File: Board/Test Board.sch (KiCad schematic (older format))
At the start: 29 parts, among them J1 SCREW TERMINAL, J2 SCREW TERMINAL, J3 SCREW TERMINAL, K1 FINDER-32.21-x300, K2 FINDER-32.21-x300, K3 FINDER-32.21-x300, SW1 UP-MJTP1230, SW2 LT-MJTP1230, SW3 DN-MJTP1230, SW4 RT-MJTP1230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

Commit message: Begin the process of a design shrink
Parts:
- removed A1: Arduino_Nano_v3.x, Module:Arduino_Nano, symbol Test-Board-rescue:Arduino_Nano_v3.x-MCU_Module
- removed K1, K2, K3: FINDER-32.21-x300, Relay_THT:Relay_SPST_Finder_32.21-x300, symbol Relay:FINDER-32.21-x300
- added A1: Arduino_Nano_v3.x, Module:Arduino_Nano, symbol MCU_Module:Arduino_Nano_v3.x
- added U3, U4, U5: DS1E-M-DC5V, Arduino-Thermostat:DS1E-M-DC5V, symbol Arduino-Thermostat:DS1E-M-DC5V
- C1, C2: value 680uF -> 220uF; footprint Capacitor_THT:CP_Radial_D12.5mm_P5.00mm -> Capacitor_THT:CP_Radial_D10.0mm_P5.00mm
- D2: value SB5199TA -> 31DQ05TA; footprint Diode_THT:D_DO-201_P15.24mm_Horizontal -> Diode_THT:D_DO-201AD_P5.08mm_Vertical_AnodeUp
- L1: value 53uH -> 100uH
- R23: value 220R -> 600R
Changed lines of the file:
@@
 P 1450 1350
 F 0 "C1" H 1568 1396 50  0000 L CNN
-F 1 "680uF" H 1568 1305 50  0000 L CNN
-F 2 "Capacitor_THT:CP_Radial_D12.5mm_P5.00mm" H 1488 1200 50  0001 C CNN
+F 1 "220uF" H 1568 1305 50  0000 L CNN
+F 2 "Capacitor_THT:CP_Radial_D10.0mm_P5.00mm" H 1488 1200 50  0001 C CNN
 F 3 "~" H 1450 1350 50  0001 C CNN
 	1    1450 1350
@@
 P 3350 1550
 F 0 "C2" H 3468 1596 50  0000 L CNN
-F 1 "680uF" H 3468 1505 50  0000 L CNN
-F 2 "Capacitor_THT:CP_Radial_D12.5mm_P5.00mm" H 3388 1400 50  0001 C CNN
+F 1 "220uF" H 3468 1505 50  0000 L CNN
+F 2 "Capacitor_THT:CP_Radial_D10.0mm_P5.00mm" H 3388 1400 50  0001 C CNN
 F 3 "~" H 3350 1550 50  0001 C CNN
 	1    3350 1550
@@
 P 2850 1550
 F 0 "D2" V 2804 1630 50  0000 L CNN
-F 1 "SB5199TA" V 2895 1630 50  0000 L CNN
-F 2 "Diode_THT:D_DO-201_P15.24mm_Horizontal" H 2850 1550 50  0001 C CNN
+F 1 "31DQ05TA" V 2895 1630 50  0000 L CNN
+F 2 "Diode_THT:D_DO-201AD_P5.08mm_Vertical_AnodeUp" H 2850 1550 50  0001 C CNN
 F 3 "~" H 2850 1550 50  0001 C CNN
 	1    2850 1550
@@
 P 3200 1400
 F 0 "L1" V 3390 1400 50  0000 C CNN
-F 1 "53uH" V 3299 1400 50  0000 C CNN
+F 1 "100uH" V 3299 1400 50  0000 C CNN
 F 2 "Inductor_THT:L_Toroid_Vertical_L21.6mm_W11.4mm_P7.62mm_Pulse_KM-3" H 3200 1400 50  0001 C CNN
 F 3 "~" H 3200 1400 50  0001 C CNN
@@
 	1    1650 5350
 	-1   0    0    -1
-$EndComp
-$Comp
-L Test-Board-rescue:Arduino_Nano_v3.x-MCU_Module A1
-U 1 1 6118DE62
-P 10200 1800
-F 0 "A1" H 10200 711 50  0000 C CNN
-F 1 "Arduino_Nano_v3.x" H 10200 620 50  0000 C CNN
-F 2 "Module:Arduino_Nano" H 10200 1800 50  0001 C CIN
-F 3 "http://www.mouser.com/pdfdocs/Gravitech_Arduino_Nano3_0.pdf" H 10200 1800 50  0001 C CNN
-	1    10200 1800
-	1    0    0    -1
 $EndComp
 $Comp
@@
 Wire Wire Line
 	10200 4400 10350 4400
-Wire Wire Line
-	10300 2800 10200 2800
-Wire Wire Line
-	10200 2800 9800 2800
-Connection ~ 10200 2800
 $Comp
 L power:GND #PWR0120
@@
 P 5100 2300
 F 0 "R23" H 5170 2346 50  0000 L CNN
-F 1 "220R" H 5170 2255 50  0000 L CNN
+F 1 "600R" H 5170 2255 50  0000 L CNN
 F 2 "Resistor_THT:R_Axial_DIN0207_L6.3mm_D2.5mm_P7.62mm_Horizontal" V 5030 2300 50  0001 C CNN
 F 3 "~" H 5100 2300 50  0001 C CNN
@@
 	0    -1   -1   0
 $EndComp
-$Comp
-L Relay:FINDER-32.21-x300 K1
-U 1 1 612C8E7E
-P 3800 4300
-F 0 "K1" H 4230 4346 50  0000 L CNN
-F 1 "FINDER-32.21-x300" H 4230 4255 50  0000 L CNN
-F 2 "Relay_THT:Relay_SPST_Finder_32.21-x300" H 5070 4270 50  0001 C CNN
-F 3 "http://gfinder.findernet.com/assets/Series/355/S32EN.pdf" H 3800 4300 50  0001 C CNN
-	1    3800 4300
-	1    0    0    -1
-$EndComp
-$Comp
-L Relay:FINDER-32.21-x300 K3
-U 1 1 612D0CAA
-P 3800 6300
-F 0 "K3" H 4230 6346 50  0000 L CNN
-F 1 "FINDER-32.21-x300" H 4230 6255 50  0000 L CNN
-F 2 "Relay_THT:Relay_SPST_Finder_32.21-x300" H 5070 6270 50  0001 C CNN
-F 3 "http://gfinder.findernet.com/assets/Series/355/S32EN.pdf" H 3800 6300 50  0001 C CNN
-	1    3800 6300
-	1    0    0    -1
-$EndComp
-$Comp
-L Relay:FINDER-32.21-x300 K2
-U 1 1 612D5FFC
-P 3800 5300
-F 0 "K2" H 4230 5346 50  0000 L CNN
-F 1 "FINDER-32.21-x300" H 4230 5255 50  0000 L CNN
-F 2 "Relay_THT:Relay_SPST_Finder_32.21-x300" H 5070 5270 50  0001 C CNN
-F 3 "http://gfinder.findernet.com/assets/Series/355/S32EN.pdf" H 3800 5300 50  0001 C CNN
-	1    3800 5300
-	1    0    0    -1
-$EndComp
-Text Label 4250 4000 0    50   ~ 0
+Text Label 4300 4750 0    50   ~ 0
 R
-Text Label 4250 5000 0    50   ~ 0
+Text Label 4300 6100 0    50   ~ 0
 R
-Text Label 4250 6000 0    50   ~ 0
-R
-Wire Wire Line
-	4100 6000 4250 6000
-Wire Wire Line
-	4100 5000 4250 5000
-Wire Wire Line
-	4100 4000 4250 4000
+Wire Wire Line
+	4150 6100 4300 6100
+Wire Wire Line
+	4150 4750 4300 4750
 $Comp
 L power:GND #PWR03
 U 1 1 6132FB03
-P 3600 6600
-F 0 "#PWR03" H 3600 6350 50  0001 C CNN
-F 1 "GND" H 3605 6427 50  0000 C CNN
-F 2 "" H 3600 6600 50  0001 C CNN
-F 3 "" H 3600 6600 50  0001 C CNN
-	1    3600 6600
-	1    0    0    -1
-$EndComp
-$Comp
-L power:GND #PWR02
-U 1 1 613309E2
-P 3600 5600
-F 0 "#PWR02" H 3600 5350 50  0001 C CNN
-F 1 "GND" H 3605 5427 50  0000 C CNN
-F 2 "" H 3600 5600 50  0001 C CNN
-F 3 "" H 3600 5600 50  0001 C CNN
-	1    3600 5600
+P 3800 7100
+F 0 "#PWR03" H 3800 6850 50  0001 C CNN
+F 1 "GND" H 3805 6927 50  0000 C CNN
+F 2 "" H 3800 7100 50  0001 C CNN
+F 3 "" H 3800 7100 50  0001 C CNN
+	1    3800 7100
 	1    0    0    -1
 $EndComp
@@
 L power:GND #PWR01
 U 1 1 61331D39
-P 3600 4600
-F 0 "#PWR01" H 3600 4350 50  0001 C CNN
-F 1 "GND" H 3605 4427 50  0000 C CNN
-F 2 "" H 3600 4600 50  0001 C CNN
-F 3 "" H 3600 4600 50  0001 C CNN
-	1    3600 4600
-	1    0    0    -1
-$EndComp
-Text Label 3900 4000 2    50   ~ 0
+P 3800 4400
+F 0 "#PWR01" H 3800 4150 50  0001 C CNN
+F 1 "GND" H 3805 4227 50  0000 C CNN
+F 2 "" H 3800 4400 50  0001 C CNN
+F 3 "" H 3800 4400 50  0001 C CNN
+	1    3800 4400
+	1    0    0    -1
+$EndComp
+Text Label 3500 3400 0    50   ~ 0
 FANRLY
-Text Label 3900 5000 2    50   ~ 0
+Text Label 3500 4750 0    50   ~ 0
 HEATRLY
-Text Label 3900 6000 2    50   ~ 0
+Text Label 3500 6100 0    50   ~ 0
 COOLRLY
 Text Label 7450 5000 2    50   ~ 0
@@
 	7050 4400 7450 4400
 Wire Wire Line
-	3600 4000 3900 4000
-Wire Wire Line
-	3600 5000 3900 5000
-Wire Wire Line
-	3600 6000 3900 6000
-Text Label 4000 6700 0    50   ~ 0
+	3800 3400 3500 3400
+Wire Wire Line
+	3800 4750 3500 4750
+Wire Wire Line
+	3800 6100 3500 6100
+Text Label 4050 7200 0    50   ~ 0
 Y
 Wire Wire Line
-	4000 6600 4000 6700
-Wire Wire Line
-	4000 5700 4000 5600
-Text Label 4000 5700 0    50   ~ 0
-W
-Text Label 4000 4700 0    50   ~ 0
+	4050 7100 4050 7200
+Text Label 4050 4500 0    50   ~ 0
 G
-Wire Wire Line
-	4000 4600 4000 4700
 $Comp
 L Connector:Screw_Terminal_01x02 J2
@@
 	0    -1   -1   0
 $EndComp
+$Comp
+L Arduino-Thermostat:DS1E-M-DC5V U3
+U 1 1 61909F87
+P 3500 5600
+F 0 "U3" V 5253 4852 60  0000 R CNN
+F 1 "DS1E-M-DC5V" V 5147 4852 60  0000 R CNN
+F 2 "Arduino-Thermostat:DS1E-M-DC5V" H 5200 5640 60  0001 C CNN
+F 3 "" H 4700 5300 60  0000 C CNN
+	1    3500 5600
+	0    -1   -1   0
+$EndComp
+Wire Wire Line
+	4050 4400 4050 4500
+Wire Wire Line
+	4150 3400 4300 3400
+Text Label 4300 3400 0    50   ~ 0
+R
+$Comp
+L Arduino-Thermostat:DS1E-M-DC5V U5
+U 1 1 619468A4
+P 3500 8300
+F 0 "U5" V 5253 7552 60  0000 R CNN
+F 1 "DS1E-M-DC5V" V 5147 7552 60  0000 R CNN
+F 2 "Arduino-Thermostat:DS1E-M-DC5V" H 5200 8340 60  0001 C CNN
+F 3 "" H 4700 8000 60  0000 C CNN
+	1    3500 8300
+	0    -1   -1   0
+$EndComp
+$Comp
+L Arduino-Thermostat:DS1E-M-DC5V U4
+U 1 1 6192B6E5
+P 3500 6950
+F 0 "U4" V 5253 6202 60  0000 R CNN
+F 1 "DS1E-M-DC5V" V 5147 6202 60  0000 R CNN
+F 2 "Arduino-Thermostat:DS1E-M-DC5V" H 5200 6990 60  0001 C CNN
+F 3 "" H 4700 6650 60  0000 C CNN
+	1    3500 6950
+	0    -1   -1   0
+$EndComp
+Text Label 4050 5850 0    50   ~ 0
+W
+Wire Wire Line
+	4050 5850 4050 5750
+$Comp
+L power:GND #PWR02
+U 1 1 613309E2
+P 3800 5750
+F 0 "#PWR02" H 3800 5500 50  0001 C CNN
+F 1 "GND" H 3805 5577 50  0000 C CNN
+F 2 "" H 3800 5750 50  0001 C CNN
+F 3 "" H 3800 5750 50  0001 C CNN
+	1    3800 5750
+	1    0    0    -1
+$EndComp
+Wire Wire Line
+	9800 2800 10200 2800
+$Comp
+L MCU_Module:Arduino_Nano_v3.x A1
+U 1 1 61970FE6
+P 10200 1800
+F 0 "A1" H 10200 711 50  0000 C CNN
+F 1 "Arduino_Nano_v3.x" H 10200 620 50  0000 C CNN
+F 2 "Module:Arduino_Nano" H 10200 1800 50  0001 C CIN
+F 3 "http://www.mouser.com/pdfdocs/Gravitech_Arduino_Nano3_0.pdf" H 10200 1800 50  0001 C CNN
+	1    10200 1800
+	1    0    0    -1
+$EndComp
+Wire Wire Line
+	10200 2800 10300 2800
+Connection ~ 10200 2800
 $EndSCHEMATC

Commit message: Started re-engineering board
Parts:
- L1: value 100uH -> 53uH; footprint Inductor_THT:L_Toroid_Vertical_L21.6mm_W11.4mm_P7.62mm_Pulse_KM-3 -> Inductor_THT:L_Radial_D12.0mm_P5.00mm_Fastron_11P
- R1: value 220R -> XXR; footprint Resistor_THT:R_Axial_DIN0207_L6.3mm_D2.5mm_P7.62mm_Horizontal -> Resistor_SMD:R_1206_3216Metric
- R18, R19, R20, R21, R22, R23: footprint Resistor_THT:R_Axial_DIN0207_L6.3mm_D2.5mm_P7.62mm_Horizontal -> Resistor_SMD:R_1206_3216Metric
- U6: footprint Sensor:Aosong_DHT11_5.5x12.0_P2.54mm -> Arduino-Thermostat:DHT22-Horizontal
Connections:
- no-connect marks 17 -> 20
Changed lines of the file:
@@
 P 3200 1400
 F 0 "L1" V 3390 1400 50  0000 C CNN
-F 1 "100uH" V 3299 1400 50  0000 C CNN
-F 2 "Inductor_THT:L_Toroid_Vertical_L21.6mm_W11.4mm_P7.62mm_Pulse_KM-3" H 3200 1400 50  0001 C CNN
+F 1 "53uH" V 3299 1400 50  0000 C CNN
+F 2 "Inductor_THT:L_Radial_D12.0mm_P5.00mm_Fastron_11P" H 3200 1400 50  0001 C CNN
 F 3 "~" H 3200 1400 50  0001 C CNN
 	1    3200 1400
@@
 F 0 "U6" V 9819 3750 50  0000 C CNN
 F 1 "DHT11" V 9910 3750 50  0000 C CNN
-F 2 "Sensor:Aosong_DHT11_5.5x12.0_P2.54mm" H 10200 3350 50  0001 C CNN
+F 2 "Arduino-Thermostat:DHT22-Horizontal" H 10200 3350 50  0001 C CNN
 F 3 "http://akizukidenshi.com/download/ds/aosong/DHT11.pdf" H 10350 4000 50  0001 C CNN
 	1    10200 3750
@@
 F 0 "R22" V 9843 4250 50  0000 C CNN
 F 1 "10k" V 9934 4250 50  0000 C CNN
-F 2 "Resistor_THT:R_Axial_DIN0207_L6.3mm_D2.5mm_P7.62mm_Horizontal" V 9980 4250 50  0001 C CNN
+F 2 "Resistor_SMD:R_1206_3216Metric" V 9980 4250 50  0001 C CNN
 F 3 "~" H 10050 4250 50  0001 C CNN
 	1    10050 4250
@@
 F 0 "R20" H 10020 5096 50  0000 L CNN
 F 1 "47k" H 10020 5005 50  0000 L CNN
-F 2 "Resistor_THT:R_Axial_DIN0207_L6.3mm_D2.5mm_P7.62mm_Horizontal" V 9880 5050 50  0001 C CNN
+F 2 "Resistor_SMD:R_1206_3216Metric" V 9880 5050 50  0001 C CNN
 F 3 "~" H 9950 5050 50  0001 C CNN
 	1    9950 5050
@@
 F 0 "R18" H 8870 5096 50  0000 L CNN
 F 1 "47k" H 8870 5005 50  0000 L CNN
-F 2 "Resistor_THT:R_Axial_DIN0207_L6.3mm_D2.5mm_P7.62mm_Horizontal" V 8730 5050 50  0001 C CNN
+F 2 "Resistor_SMD:R_1206_3216Metric" V 8730 5050 50  0001 C CNN
 F 3 "~" H 8800 5050 50  0001 C CNN
 	1    8800 5050
@@
 F 0 "R19" H 8870 5796 50  0000 L CNN
 F 1 "47k" H 8870 5705 50  0000 L CNN
-F 2 "Resistor_THT:R_Axial_DIN0207_L6.3mm_D2.5mm_P7.62mm_Horizontal" V 8730 5750 50  0001 C CNN
+F 2 "Resistor_SMD:R_1206_3216Metric" V 8730 5750 50  0001 C CNN
 F 3 "~" H 8800 5750 50  0001 C CNN
 	1    8800 5750
@@
 F 0 "R21" H 10020 5796 50  0000 L CNN
 F 1 "47k" H 10020 5705 50  0000 L CNN
-F 2 "Resistor_THT:R_Axial_DIN0207_L6.3mm_D2.5mm_P7.62mm_Horizontal" V 9880 5750 50  0001 C CNN
+F 2 "Resistor_SMD:R_1206_3216Metric" V 9880 5750 50  0001 C CNN
 F 3 "~" H 9950 5750 50  0001 C CNN
 	1    9950 5750
@@
 F 0 "R23" H 5170 2346 50  0000 L CNN
 F 1 "600R" H 5170 2255 50  0000 L CNN
-F 2 "Resistor_THT:R_Axial_DIN0207_L6.3mm_D2.5mm_P7.62mm_Horizontal" V 5030 2300 50  0001 C CNN
+F 2 "Resistor_SMD:R_1206_3216Metric" V 5030 2300 50  0001 C CNN
 F 3 "~" H 5100 2300 50  0001 C CNN
 	1    5100 2300
@@
 P 7700 1900
 F 0 "R1" V 7907 1900 50  0000 C CNN
-F 1 "220R" V 7816 1900 50  0000 C CNN
-F 2 "Resistor_THT:R_Axial_DIN0207_L6.3mm_D2.5mm_P7.62mm_Horizontal" V 7630 1900 50  0001 C CNN
+F 1 "XXR" V 7816 1900 50  0000 C CNN
+F 2 "Resistor_SMD:R_1206_3216Metric" V 7630 1900 50  0001 C CNN
 F 3 "~" H 7700 1900 50  0001 C CNN
 	1    7700 1900
@@
 	10200 2800 10300 2800
 Connection ~ 10200 2800
+NoConn ~ 3900 3400
+NoConn ~ 3900 4750
+NoConn ~ 3900 6100
 $EndSCHEMATC

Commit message: Added E-Ink Display files
Started making E-Ink Display footprints
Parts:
- removed DS1: WC1602A, Display:WC1602A, symbol Display_Character:WC1602A
- removed R1: XXR, Resistor_SMD:R_1206_3216Metric, symbol Device:R
- removed R18, R19, R20, R21: 47k, Resistor_SMD:R_1206_3216Metric, symbol Device:R
- removed RV1: 10k, Potentiometer_THT:Potentiometer_Bourns_3266Y_Vertical, symbol Device:R_POT
- removed SW1: UP-MJTP1230, Button_Switch_THT:SW_PUSH_6mm, symbol Switch:SW_Push
- removed SW2: LT-MJTP1230, Button_Switch_THT:SW_PUSH_6mm, symbol Switch:SW_Push
- removed SW3: DN-MJTP1230, Button_Switch_THT:SW_PUSH_6mm, symbol Switch:SW_Push
- removed SW4: RT-MJTP1230, Button_Switch_THT:SW_PUSH_6mm, symbol Switch:SW_Push
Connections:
- wire segments 87 -> 65
- no-connect marks 20 -> 16
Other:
- moved on the sheet: D3, R23, U2

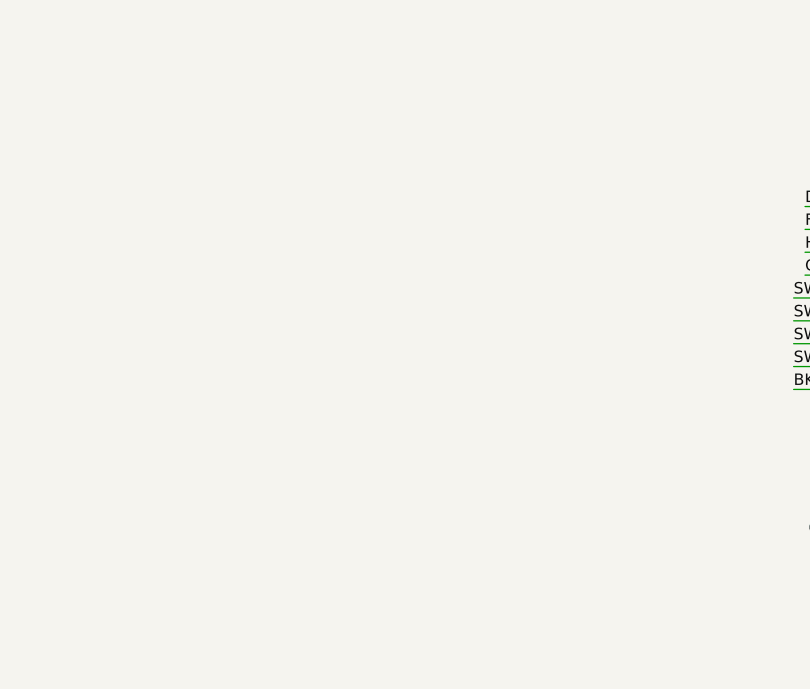
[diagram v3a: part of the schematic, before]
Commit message: Finished E-Ink Footprint
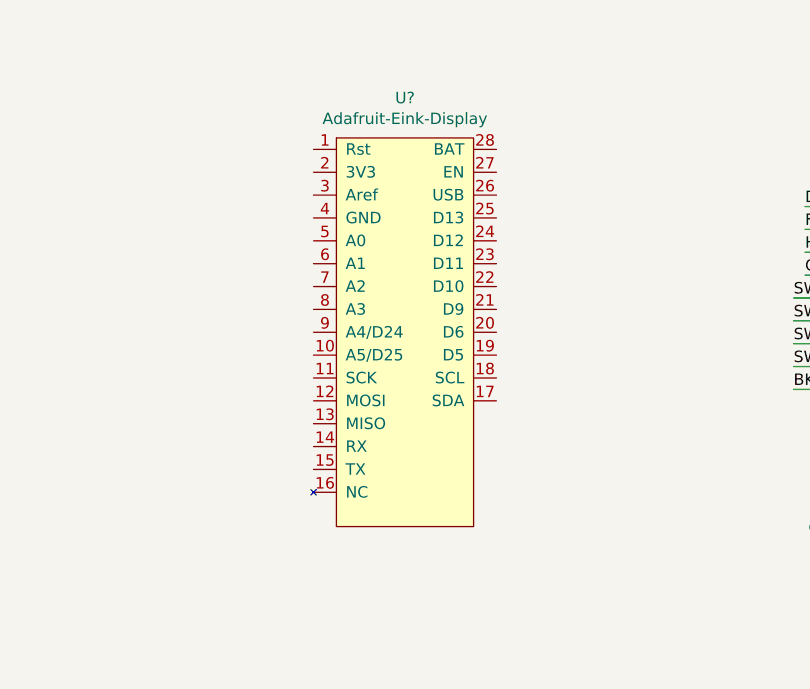
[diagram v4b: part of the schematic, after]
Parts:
- added U?: Adafruit-Eink-Display, symbol Arduino-Thermostat:Adafruit-Eink-Display
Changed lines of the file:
@@
 NoConn ~ 3900 4750
 NoConn ~ 3900 6100
+$Comp
+L Arduino-Thermostat:Adafruit-Eink-Display U?
+U 1 1 61ED981D
+P 7750 1050
+F 0 "U?" H 7750 1175 50  0000 C CNN
+F 1 "Adafruit-Eink-Display" H 7750 1084 50  0000 C CNN
+F 2 "" H 7750 1050 50  0001 C CNN
+F 3 "" H 7750 1050 50  0001 C CNN
+	1    7750 1050
+	1    0    0    -1
+$EndComp
 $EndSCHEMATC

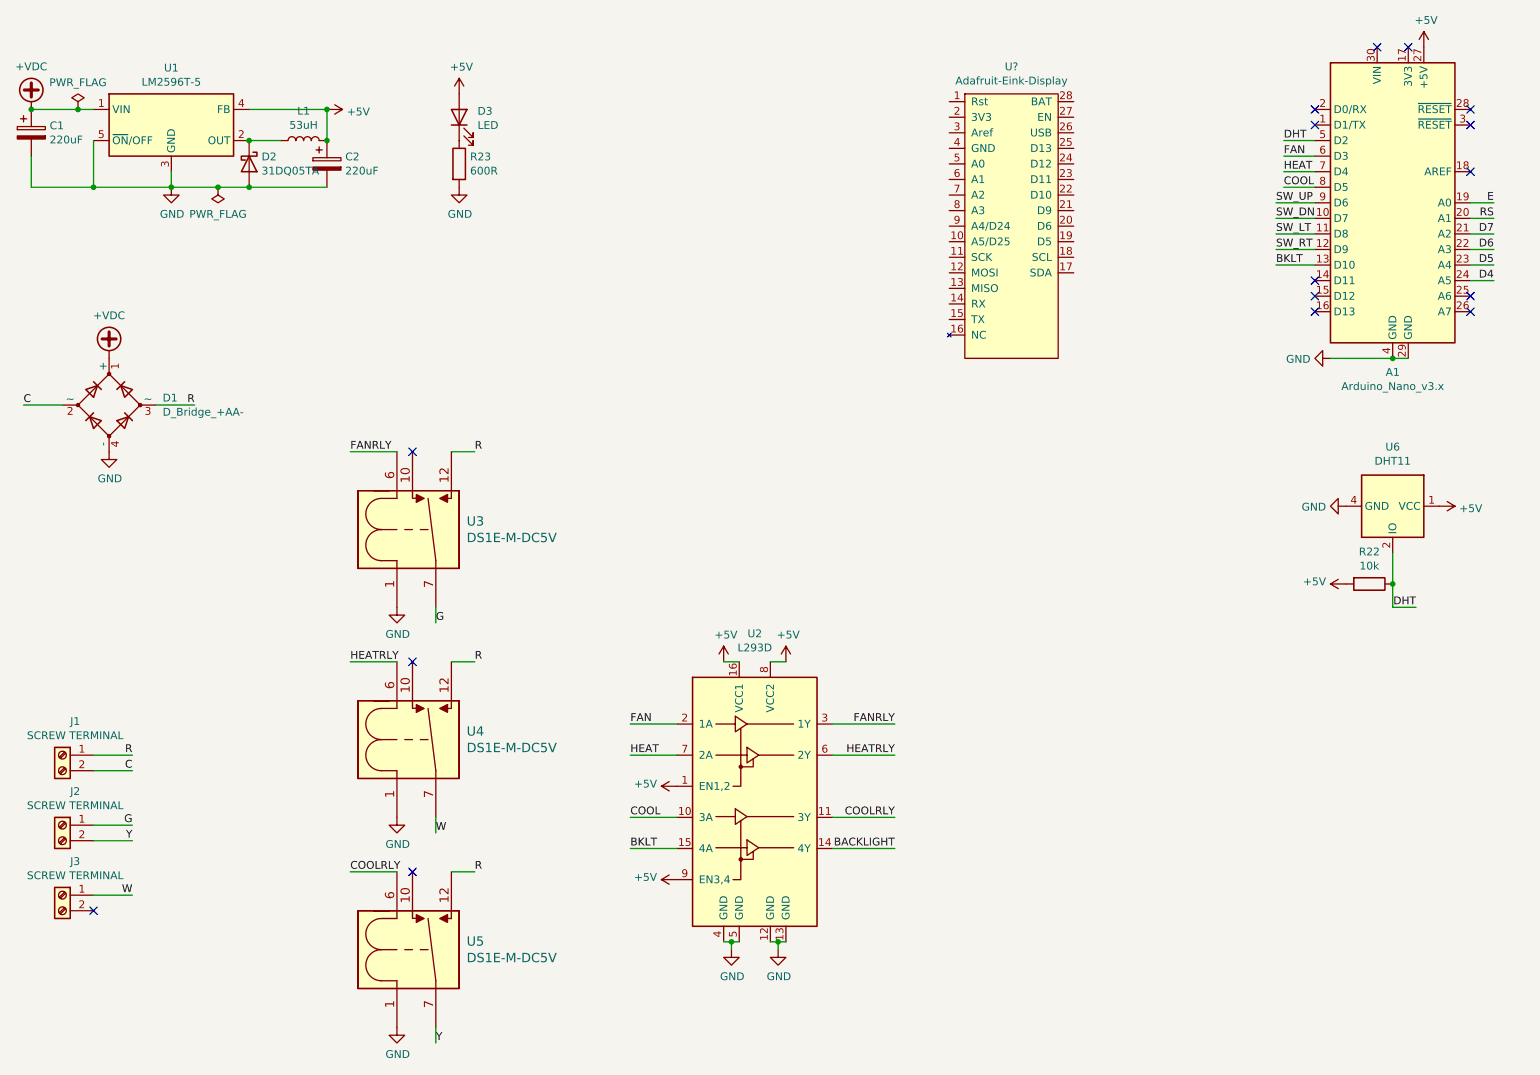
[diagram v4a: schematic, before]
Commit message: Added Feather Symbol
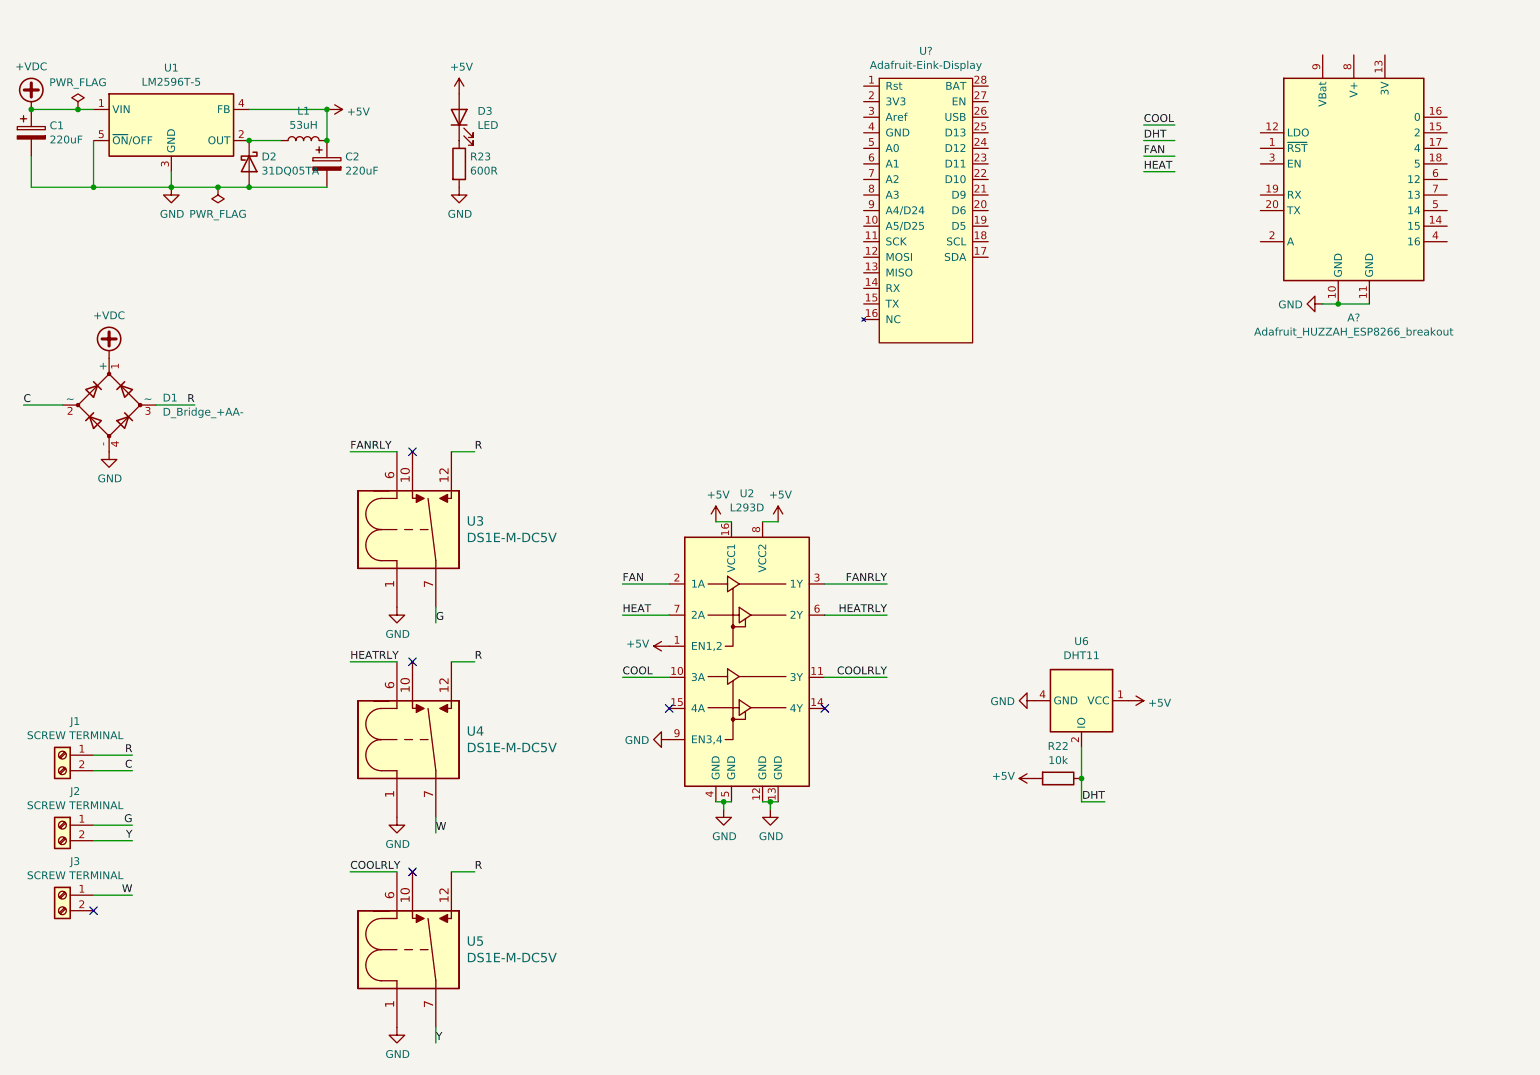
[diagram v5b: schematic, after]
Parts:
- removed A1: Arduino_Nano_v3.x, Module:Arduino_Nano, symbol MCU_Module:Arduino_Nano_v3.x
- added A?: Adafruit_HUZZAH_ESP8266_breakout, symbol MCU_Module:Adafruit_HUZZAH_ESP8266_breakout
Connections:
- net labels removed: BACKLIGHT, BKLT, D4, D5, D6, D7, E, RS, SW_DN, SW_LT, SW_RT, SW_UP
- wire segments 65 -> 52
- no-connect marks 16 -> 6
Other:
- moved on the sheet: R22, U2, U6, U?
